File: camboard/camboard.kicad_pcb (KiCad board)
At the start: 2 copper layers, 60 parts, among them J1 USB_microB_2040002-1, J2 Micro_SD_Card, J3 PPTC102LFBN-RC, J4 Conn_ARM_JTAG_SWD_20, J5 GS2, J6 Conn_02x25_Row_Letter_First, SW1 SW_DPDT_x2, SW2 SW_Push, SW3 SW_Push, SW4 SW_DPDT_x2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

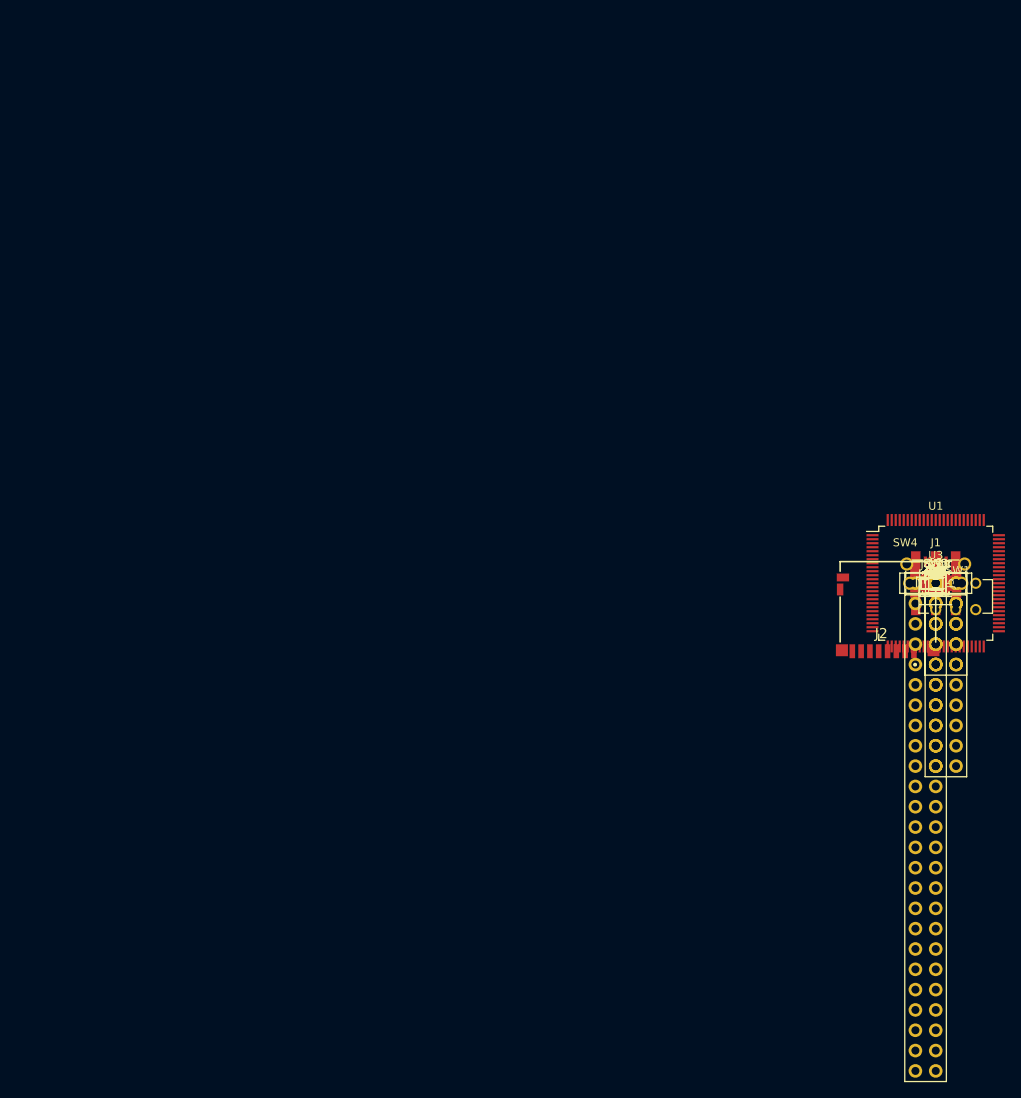
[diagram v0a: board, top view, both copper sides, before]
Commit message: Placed components (for now)
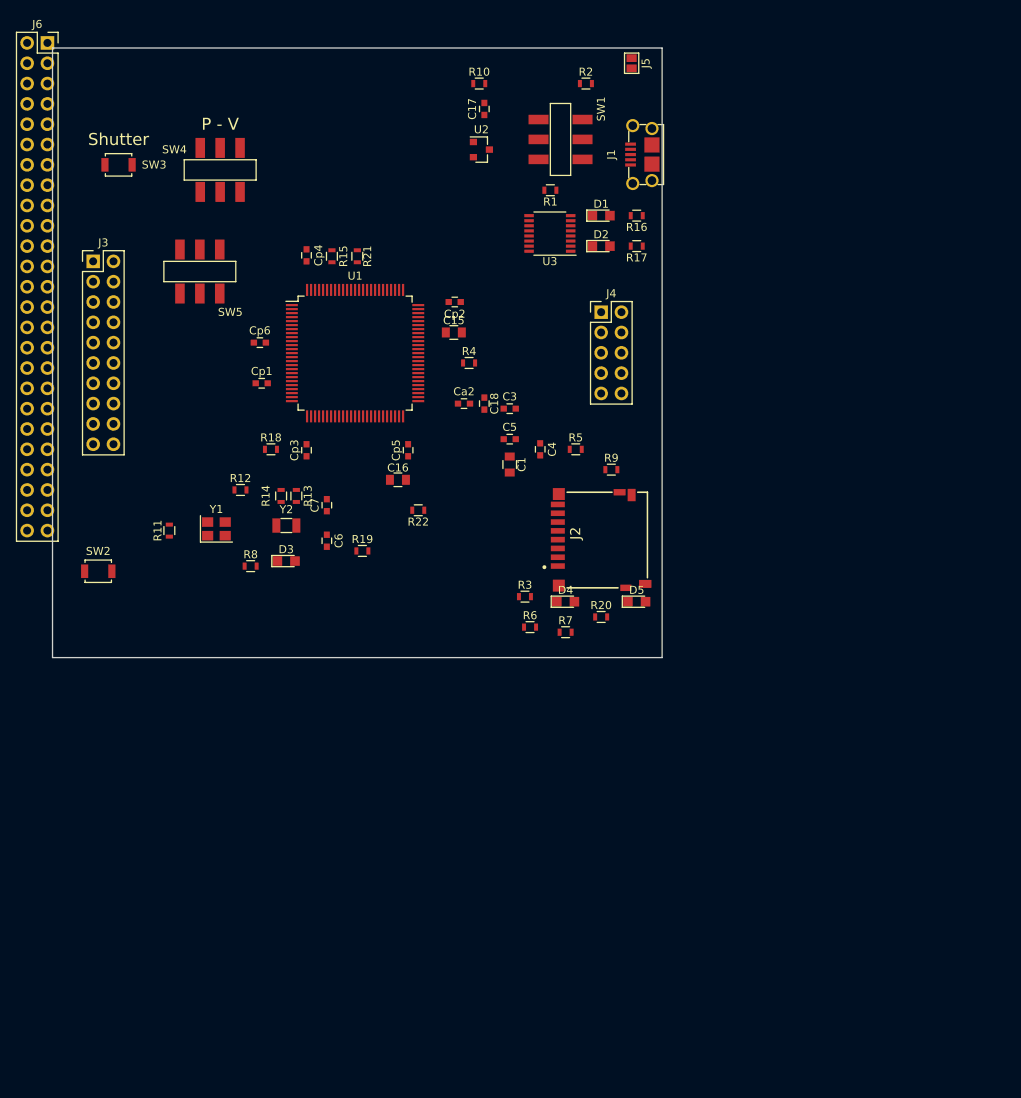
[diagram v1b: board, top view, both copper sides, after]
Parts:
- removed C10, C11, C12, C13, C14, C8, C9: 100nF, Capacitors_SMD:C_0603
- removed C2: 1uF, Capacitors_SMD:C_0603
- added Ca2: 1uF, Capacitors_SMD:C_0603, F.Cu at (89.5, 82.5)
- added Cp1: 100nF, Capacitors_SMD:C_0603, F.Cu at (64.2, 80.0)
- added Cp2: 100nF, Capacitors_SMD:C_0603, F.Cu at (88.4, 69.8)
- added Cp3: 100nF, Capacitors_SMD:C_0603, F.Cu at (69.8, 88.4)
- added Cp4: 100nF, Capacitors_SMD:C_0603, F.Cu at (69.8, 64.0)
- added Cp5: 100nF, Capacitors_SMD:C_0603, F.Cu at (82.5, 88.4)
- added Cp6: 100nF, Capacitors_SMD:C_0603, F.Cu at (64.0, 74.9)
- added SW5: SW_DPDT_x2, DPDT_switch:JS202011SCQN, F.Cu at (56.5, 66.0)
- C6, C7: value 100nF -> 4.7pF
- SW1: footprint Buttons_Switches_THT:SW_CuK_JS202011CQN_DPDT_Straight -> DPDT_switch:JS202011SCQN
- moved J6 130.0 mm to (37.5, 37.5)
- moved SW3 114.8 mm to (46.4, 52.7)
- moved J3 112.7 mm to (43.2, 64.8)
- moved SW2 104.7 mm to (43.8, 103.5)
- moved SW4 103.3 mm to (59.1, 53.3)
- moved R11 96.0 mm to (52.7, 98.4), turned to 90 degrees
- moved Y1 90.2 mm to (58.6, 98.2)
- moved R12 87.7 mm to (61.6, 93.3)
- moved R15 85.8 mm to (73.0, 64.1), turned to 270 degrees
- moved R8 85.7 mm to (62.9, 102.9)
- moved R18 84.8 mm to (65.4, 88.3)
- moved R10 84.6 mm to (91.4, 42.5)
- moved R21 83.1 mm to (76.2, 64.1), turned to 90 degrees
- moved R14 82.6 mm to (66.7, 94.1), turned to 270 degrees
- moved C17 81.8 mm to (92.1, 45.7), turned to 90 degrees
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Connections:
- C5 pad 1: +3V3 -> GND
- C5 pad 2: GND -> +3V3
- J3 pad 17: Net-(J3-Pad17) -> (no net)
- J3 pad 18: Net-(J3-Pad18) -> (no net)
- J3 pad 8: /OSC25M -> /CLK
- R10 pad 1: Net-(J4-Pad11) -> (no net)
- R11 pad 1: +3V3 -> Net-(R11-Pad1)
- R11 pad 2: Net-(R11-Pad2) -> +3V3
- R12 pad 2: /OSC25M -> Net-(R12-Pad2)
- R8 pad 1: Net-(J4-Pad17) -> (no net)
- R9 pad 1: Net-(J4-Pad19) -> (no net)
- SW1 pad 4: +3V3 -> /USB_5V
- SW1 pad 5: Net-(R15-Pad1) -> Net-(C17-Pad1)
- SW1 pad 6: GND -> /VIN
- SW4 pad 4: (no net) -> GND
- SW4 pad 5: (no net) -> Net-(R22-Pad1)
- SW4 pad 6: (no net) -> +3V3
- U1 pad 12: /OSC25M -> Net-(R12-Pad2)
- U1 pad 13: Net-(U1-Pad13) -> (no net)
- U1 pad 15: Net-(J6-Padb4) -> (no net)
- U1 pad 16: Net-(J6-Padb5) -> (no net)
- U1 pad 17: Net-(J6-Padb6) -> (no net)
- U1 pad 18: Net-(J6-Padb7) -> (no net)
- U1 pad 24: Net-(J6-Padb8) -> (no net)
- U1 pad 25: Net-(J6-Padb9) -> (no net)
- U1 pad 29: Net-(J6-Padb10) -> (no net)
- U1 pad 31: Net-(J6-Padb11) -> (no net)
- U1 pad 32: Net-(J6-Padb12) -> (no net)
- U1 pad 33: Net-(J6-Padb13) -> (no net)
- U1 pad 34: Net-(J6-Padb14) -> (no net)
- U1 pad 35: Net-(J6-Padb15) -> (no net)
- U1 pad 36: Net-(J6-Padb16) -> (no net)
- U1 pad 37: Net-(J6-Padb17) -> (no net)
- U1 pad 38: Net-(J6-Padb18) -> (no net)
- U1 pad 39: Net-(J6-Padb19) -> (no net)
- U1 pad 40: Net-(J6-Padb20) -> (no net)
- U1 pad 41: Net-(J6-Pada21) -> (no net)
- U1 pad 42: Net-(J6-Pada20) -> (no net)
- U1 pad 43: Net-(J6-Pada19) -> (no net)
- U1 pad 44: Net-(J6-Pada18) -> (no net)
- U1 pad 45: Net-(J6-Pada17) -> (no net)
- U1 pad 51: Net-(J6-Pada16) -> (no net)
- U1 pad 52: Net-(J6-Pada15) -> (no net)
- U1 pad 53: Net-(J6-Pada14) -> (no net)
- U1 pad 54: Net-(J6-Pada13) -> (no net)
- U1 pad 57: Net-(J6-Pada12) -> (no net)
- U1 pad 6: Net-(U1-Pad6) -> (no net)
- U1 pad 60: Net-(J6-Pada11) -> (no net)
- U1 pad 61: Net-(J6-Pada10) -> (no net)
- U1 pad 62: Net-(J6-Pada9) -> (no net)
- U1 pad 63: Net-(U1-Pad63) -> (no net)
- U1 pad 64: Net-(U1-Pad64) -> (no net)
- U1 pad 67: Net-(J6-Pada8) -> /CLK
- U1 pad 7: Net-(J6-Padb3) -> (no net)
- U1 pad 70: Net-(J6-Pada7) -> (no net)
- U1 pad 71: Net-(J6-Pada6) -> (no net)
- U1 pad 81: Net-(J6-Pada5) -> (no net)
- U1 pad 82: Net-(J6-Pada4) -> (no net)
- U1 pad 85: Net-(J6-Pada3) -> (no net)
- U1 pad 87: Net-(U1-Pad87) -> (no net)
- U1 pad 89: Net-(J4-Pad13) -> (no net)
- U1 pad 91: Net-(U1-Pad91) -> (no net)
- U1 pad 92: Net-(U1-Pad92) -> (no net)
- U1 pad 95: Net-(U1-Pad95) -> (no net)
- U1 pad 96: Net-(U1-Pad96) -> (no net)
- U3 pad 10: Net-(U3-Pad10) -> (no net)
- U3 pad 15: Net-(U3-Pad15) -> (no net)
- U3 pad 16: Net-(U3-Pad16) -> (no net)
- Y1 pad 1: Net-(R11-Pad2) -> Net-(R11-Pad1)
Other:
- board outline added: 76.2 x 76.2 mm
- board text added: "P - V"
- board text added: "Shutter"

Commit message: Finished(ish) placing components
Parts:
- added J7: Conn_01x25_Female, Pin_Headers:Pin_Header_Straight_1x25_Pitch2.54mm, F.Cu at (42.5, 40.6)
- J6: value Conn_02x25_Row_Letter_First -> Conn_01x25_Female; footprint Socket_Strips:Socket_Strip_Straight_2x25_Pitch2.54mm -> Pin_Headers:Pin_Header_Straight_1x25_Pitch2.54mm
- moved J6 99.4 mm to (103.5, 111.8), turned to 270 degrees
- moved R8 59.7 mm to (118.2, 80.6)
- moved R10 43.3 mm to (120.0, 75.0), turned to 90 degrees
- moved C1 40.6 mm to (84.5, 51.1)
- moved C18 31.9 mm to (87.6, 50.9)
- moved Ca2 25.9 mm to (63.6, 81.9)
- moved R2 13.3 mm to (104.8, 55.9)
- moved R9 13.2 mm to (119.5, 84.5)
- moved D4 9.67 mm to (93.3, 103.5)
- moved R20 9.67 mm to (97.8, 105.4)
- moved R3 9.67 mm to (88.3, 102.9)
- moved R7 9.67 mm to (93.3, 107.3)
- moved R6 9.67 mm to (88.9, 106.7)
- moved J5 5.12 mm to (111.1, 45.1), turned to 270 degrees
- moved C16 4.28 mm to (78.7, 88.6), turned to 270 degrees
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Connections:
- J6 pad 1: (no net) -> GND
- J6 pad 10: (no net) -> Net-(J6-Pad10)
- J6 pad 11: (no net) -> Net-(J6-Pad11)
- J6 pad 12: (no net) -> Net-(J6-Pad12)
- J6 pad 13: (no net) -> Net-(J6-Pad13)
- J6 pad 14: (no net) -> Net-(J6-Pad14)
- J6 pad 15: (no net) -> Net-(J6-Pad15)
- J6 pad 16: (no net) -> Net-(J6-Pad16)
- J6 pad 17: (no net) -> Net-(J6-Pad17)
- J6 pad 18: (no net) -> Net-(J6-Pad18)
- J6 pad 19: (no net) -> Net-(J6-Pad19)
- J6 pad 2: (no net) -> +3V3
- J6 pad 20: (no net) -> Net-(J6-Pad20)
- J6 pad 21: (no net) -> Net-(J6-Pad21)
- J6 pad 22: (no net) -> Net-(J6-Pad22)
- J6 pad 23: (no net) -> Net-(J6-Pad23)
- J6 pad 24: (no net) -> Net-(J6-Pad24)
- J6 pad 25: (no net) -> /DCMI_PWDN
- J6 pad 3: (no net) -> /VIN
- J6 pad 4: (no net) -> /NRST
- J6 pad 5: (no net) -> Net-(J6-Pad5)
- J6 pad 6: (no net) -> Net-(J6-Pad6)
- J6 pad 7: (no net) -> Net-(J6-Pad7)
- J6 pad 8: (no net) -> Net-(J6-Pad8)
- J6 pad 9: (no net) -> Net-(J6-Pad9)
- R18 pad 2: Net-(J6-Padb1) -> Net-(J6-Pad24)
- R19 pad 2: Net-(J6-Padb2) -> Net-(J6-Pad23)
- SW1 pad 4: /USB_5V -> /VIN
- SW1 pad 6: /VIN -> /USB_5V
- SW4 pad 4: GND -> +3V3
- SW4 pad 6: +3V3 -> GND
- SW5 pad 4: +3V3 -> GND
- SW5 pad 6: GND -> +3V3
- U1 pad 1: Net-(J6-Padb1) -> Net-(J6-Pad24)
- U1 pad 15: (no net) -> Net-(J6-Pad21)
- U1 pad 16: (no net) -> Net-(J6-Pad20)
- U1 pad 17: (no net) -> Net-(J6-Pad19)
- U1 pad 18: (no net) -> Net-(J6-Pad18)
- U1 pad 2: Net-(J6-Padb2) -> Net-(J6-Pad23)
- U1 pad 24: (no net) -> Net-(J6-Pad17)
- U1 pad 25: (no net) -> Net-(J6-Pad16)
- U1 pad 29: (no net) -> Net-(J6-Pad15)
- U1 pad 31: (no net) -> Net-(J6-Pad14)
- U1 pad 32: (no net) -> Net-(J6-Pad13)
- U1 pad 33: (no net) -> Net-(J6-Pad12)
- U1 pad 34: (no net) -> Net-(J6-Pad11)
- U1 pad 35: (no net) -> Net-(J6-Pad10)
- U1 pad 36: (no net) -> Net-(J6-Pad9)
- U1 pad 37: (no net) -> Net-(J6-Pad8)
- U1 pad 38: (no net) -> Net-(J6-Pad7)
- U1 pad 39: (no net) -> Net-(J6-Pad6)
- U1 pad 40: (no net) -> Net-(J6-Pad5)
- U1 pad 41: (no net) -> Net-(J7-Pad21)
- U1 pad 42: (no net) -> Net-(J7-Pad20)
- U1 pad 43: (no net) -> Net-(J7-Pad19)
- U1 pad 44: (no net) -> Net-(J7-Pad18)
- U1 pad 45: (no net) -> Net-(J7-Pad17)
- U1 pad 51: (no net) -> Net-(J7-Pad16)
- U1 pad 52: (no net) -> Net-(J7-Pad15)
- U1 pad 53: (no net) -> Net-(J7-Pad14)
- U1 pad 54: (no net) -> Net-(J7-Pad13)
- U1 pad 57: (no net) -> Net-(J7-Pad12)
- U1 pad 60: (no net) -> Net-(J7-Pad11)
- U1 pad 61: (no net) -> Net-(J7-Pad10)
- U1 pad 62: (no net) -> Net-(J7-Pad9)
- U1 pad 7: (no net) -> Net-(J6-Pad22)
- U1 pad 70: (no net) -> Net-(J7-Pad7)
- U1 pad 71: (no net) -> Net-(J7-Pad6)
- U1 pad 81: (no net) -> Net-(J7-Pad5)
- U1 pad 82: (no net) -> Net-(J7-Pad4)
- U1 pad 85: (no net) -> Net-(J7-Pad3)

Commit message: fixed jtag
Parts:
- J4: footprint Pin_Headers:Pin_Header_Straight_2x05_Pitch2.54mm -> Pin_Headers:Pin_Header_Straight_2x10_Pitch2.54mm
- moved D5 52.7 mm to (91.4, 58.4)
- moved R9 20.5 mm to (102.9, 72.4), turned to 180 degrees
- moved R10 19.1 mm to (101.6, 80.0)
- moved R8 18.8 mm to (100.3, 74.9)
- moved J2 3.71 mm to (110.5, 109.2)
- moved J4 2.84 mm to (108.0, 68.6)
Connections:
- J3 pad 17: (no net) -> Net-(J3-Pad17)
- J3 pad 18: (no net) -> Net-(J3-Pad18)
- R10 pad 1: (no net) -> Net-(J4-Pad11)
- R8 pad 1: (no net) -> Net-(J4-Pad17)
- R9 pad 1: (no net) -> Net-(J4-Pad19)
- U1 pad 13: (no net) -> Net-(U1-Pad13)
- U1 pad 6: (no net) -> Net-(U1-Pad6)
- U1 pad 63: (no net) -> Net-(U1-Pad63)
- U1 pad 64: (no net) -> Net-(U1-Pad64)
- U1 pad 87: (no net) -> Net-(U1-Pad87)
- U1 pad 89: (no net) -> Net-(J4-Pad13)
- U1 pad 91: (no net) -> Net-(U1-Pad91)
- U1 pad 92: (no net) -> Net-(U1-Pad92)
- U1 pad 95: (no net) -> Net-(U1-Pad95)
- U1 pad 96: (no net) -> Net-(U1-Pad96)
- U3 pad 10: (no net) -> Net-(U3-Pad10)
- U3 pad 15: (no net) -> Net-(U3-Pad15)
- U3 pad 16: (no net) -> Net-(U3-Pad16)

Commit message: better layout?
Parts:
- moved R20 47.1 mm to (94.0, 58.4)
- moved C5 44.6 mm to (52.1, 98.3), turned to 90 degrees
- moved D4 43.3 mm to (59.7, 76.2), turned to 315 degrees
- moved R22 34.1 mm to (69.8, 64.8), turned to 315 degrees
- moved R19 24.7 mm to (63.0, 80.5), turned to 45 degrees
- moved R16 18.1 mm to (94.0, 53.3), turned to 270 degrees
- moved R9 17.8 mm to (102.9, 90.2)
- moved SW2 15.9 mm to (54.2, 91.4), turned to 180 degrees
- moved SW3 15.7 mm to (59.7, 61.0), turned to 90 degrees
- moved SW5 13.2 mm to (49.6, 54.8), turned to 0 degrees
- moved R8 13.0 mm to (102.9, 87.6), turned to 180 degrees
- moved R18 12.3 mm to (77.0, 92.2), turned to 45 degrees
- moved R5 12.2 mm to (97.8, 99.1)
- moved Cp2 10.7 mm to (80.3, 63.0), turned to 225 degrees
- moved Cp5 10.6 mm to (89.2, 80.2), turned to 135 degrees
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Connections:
- J6 pad 1: GND -> Net-(J6-Pad1)
- J6 pad 2: +3V3 -> Net-(J6-Pad2)
- J6 pad 3: /VIN -> Net-(J6-Pad3)
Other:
- net class Default: clearance 0.2 -> 0.1524; trace_width 0.25 -> 0.1524; via_dia 0.6 -> 0.5842; via_drill 0.4 -> 0.381
- net class Power added: clearance 0.1524, trace_width 0.1524, via_dia 0.5842, via_drill 0.381
- rule trace_clearance: 0.2 -> 0.1524
- rule trace_min: 0.2 -> 0.1524

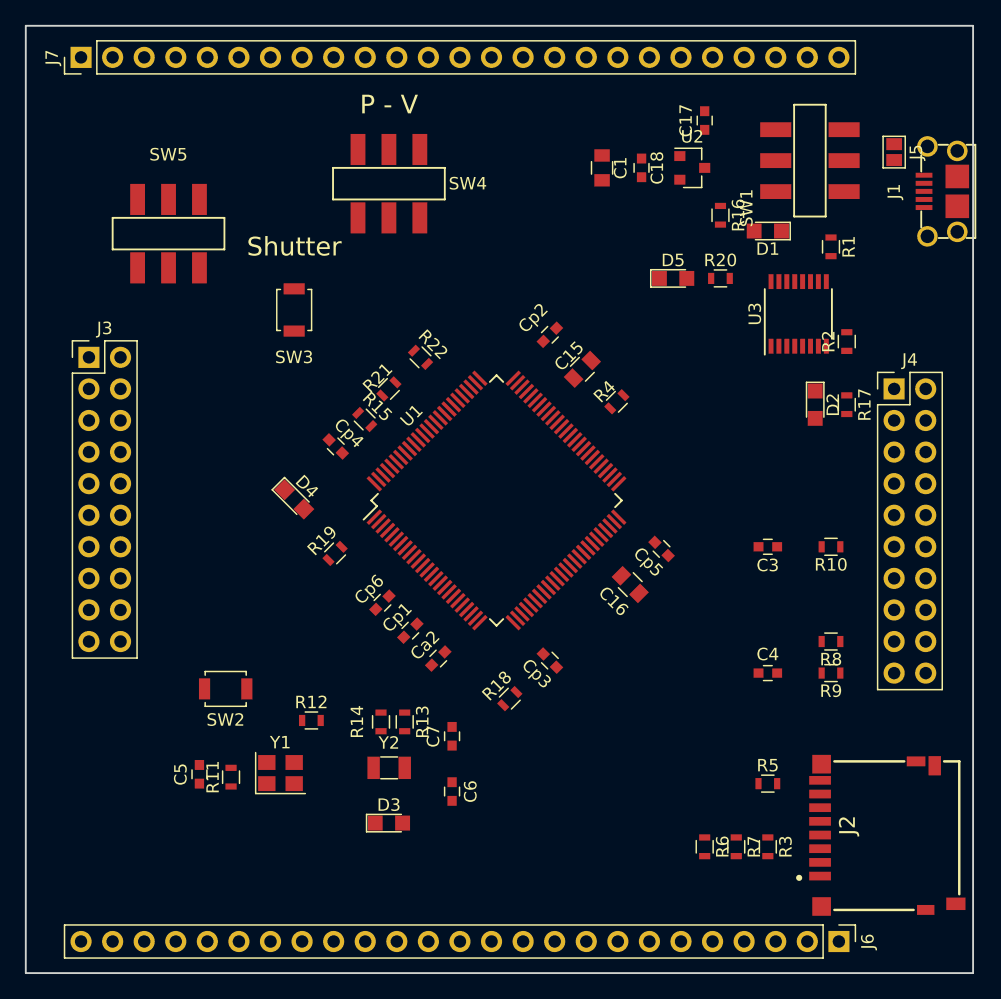
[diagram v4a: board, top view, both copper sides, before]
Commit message: auto routing attempt 3 - main processor 45 degree
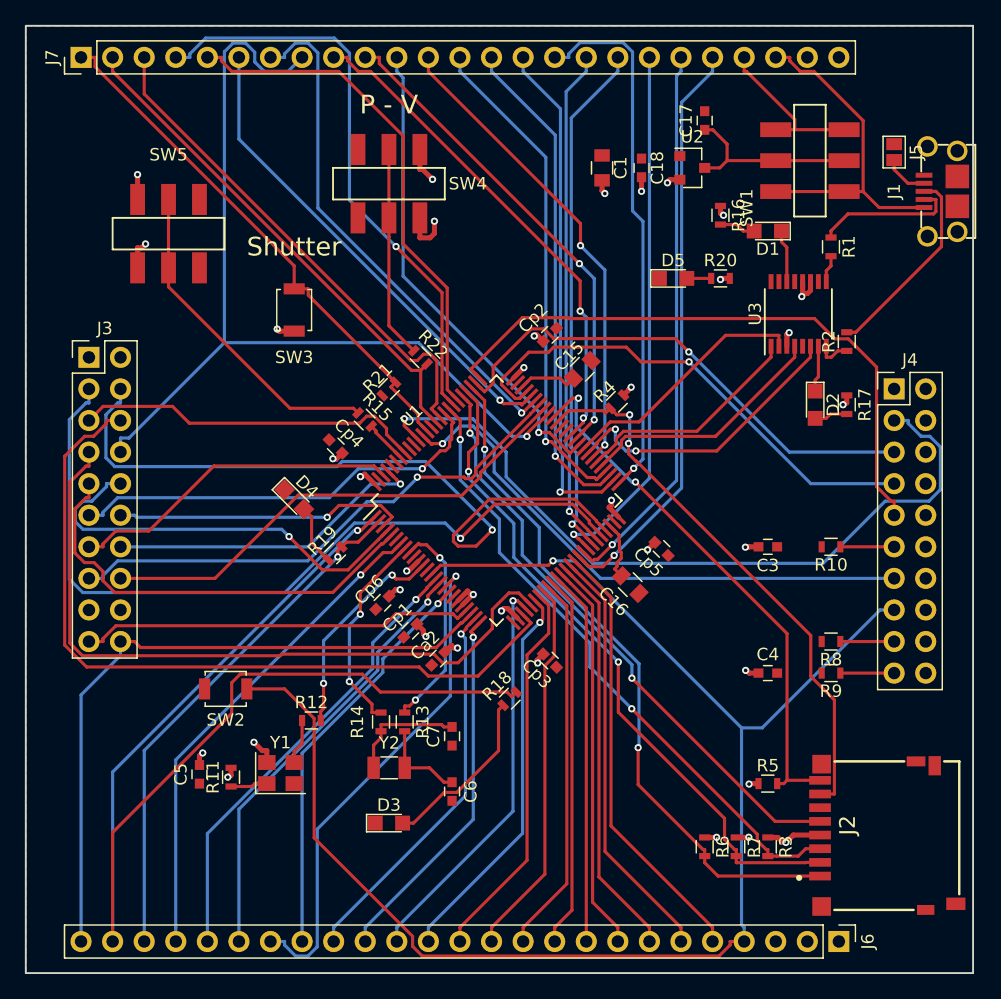
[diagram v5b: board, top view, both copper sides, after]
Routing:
- net /NRST: track 0.00 -> 120.1 mm, vias 0 -> 1
- net Net-(J6-Pad24): track 0.00 -> 92.1 mm, vias 0 -> 1
- net /CLK: track 0.00 -> 74.6 mm, vias 0 -> 1
- net Net-(J3-Pad3): track 0.00 -> 64.4 mm, vias 0 -> 1
- net Net-(J3-Pad6): track 0.00 -> 62.4 mm
- net Net-(J4-Pad3): track 0.00 -> 61.9 mm, vias 0 -> 1
- net Net-(J3-Pad4): track 0.00 -> 58.9 mm, vias 0 -> 1
- net Net-(J3-Pad7): track 0.00 -> 57.6 mm
- net Net-(J2-Pad1): track 0.00 -> 55.9 mm, vias 0 -> 2
- net +3V3: track 0.00 -> 55.3 mm, vias 0 -> 36
- net /DCMI_PWDN: track 0.00 -> 55.0 mm
- net Net-(J2-Pad2): track 0.00 -> 54.3 mm, vias 0 -> 2
- net Net-(J2-Pad3): track 0.00 -> 51.1 mm, vias 0 -> 2
- net Net-(J4-Pad9): track 0.00 -> 49.7 mm
- net Net-(J2-Pad5): track 0.00 -> 48.4 mm, vias 0 -> 2
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- added copper zone on B.Cu, net +3V3
- added copper zone on F.Cu, net GND
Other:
- net class Default: trace_width 0.1524 -> 0.254
- net class Power: trace_width 0.1524 -> 0.4064
